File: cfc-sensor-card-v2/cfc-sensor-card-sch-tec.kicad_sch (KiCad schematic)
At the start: 36 parts, among them U12 DRV8212DSGR, U13 AD5593RBCPZ-RL7, U14 MP2410A, U15 INA186A1IDCKR, U16 SN74LVC1G86DBVR, U17 SN74LVC1G08DCKR

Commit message: Processor board routing
Completed rework and routing of processor board. No drc errors or warnings. Ready for design review on processor board. Minor changes to schematic for easier routing on pull down resistors connected to the octavo SIP. Reannotated sensor schematic component designators.
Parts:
- renumbered C67 to C31, C66 to C32, C74 to C33, C68 to C34, C73 to C35, C35 to C36, C39 to C38, C69 to C39, C70 to C41, C72 to C42, C71 to C43, D5 to D4, D6 to D5, D4 to D6, R58 to R59, R66 to R60, R59 to R61, R57 to R62, R61 to R63, R62 to R64, R67 to R65, R60 to R66, R63 to R67, R71 to R68, R68 to R71, U13 to U12, U16 to U13, U17 to U14, U14 to U15, U12 to U16, U15 to U17

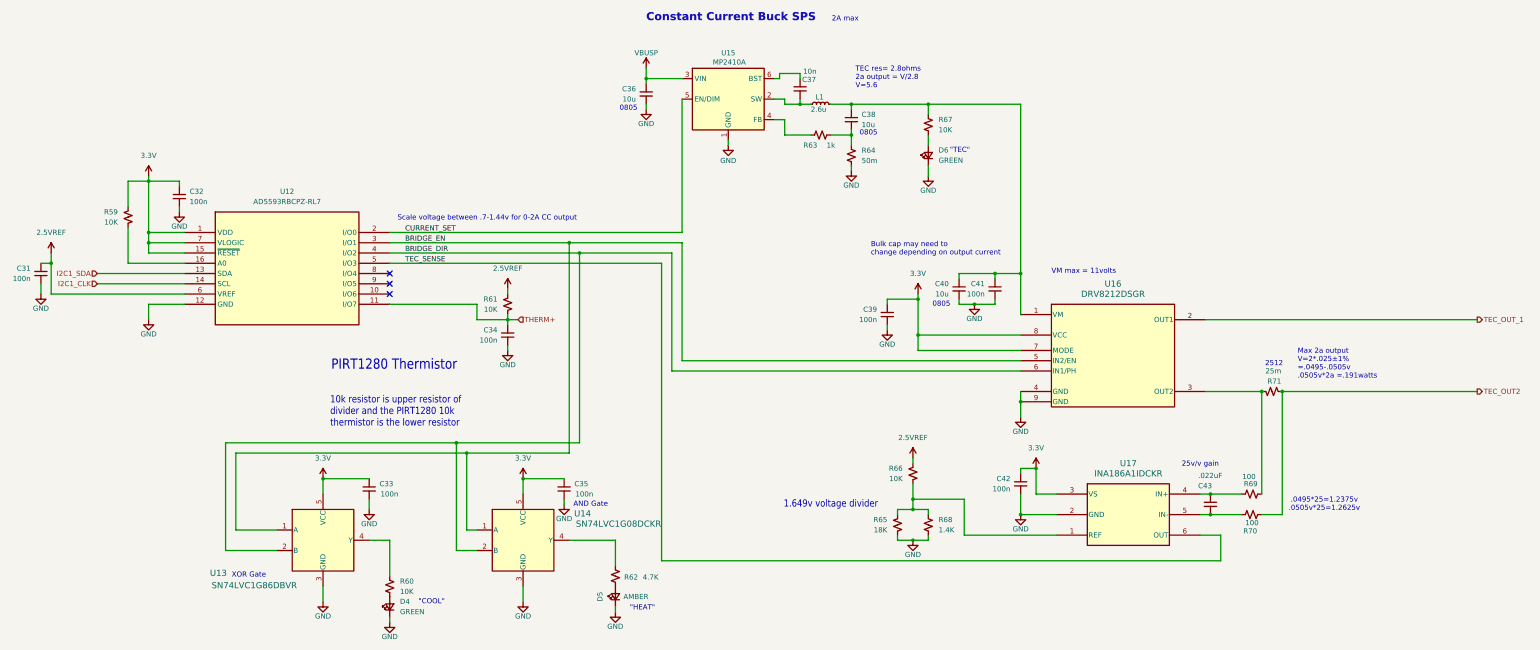
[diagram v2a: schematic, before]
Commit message: Updated OPD on sensor card
updated OPD on sensor card to match protocard. Finished placement on PCB.
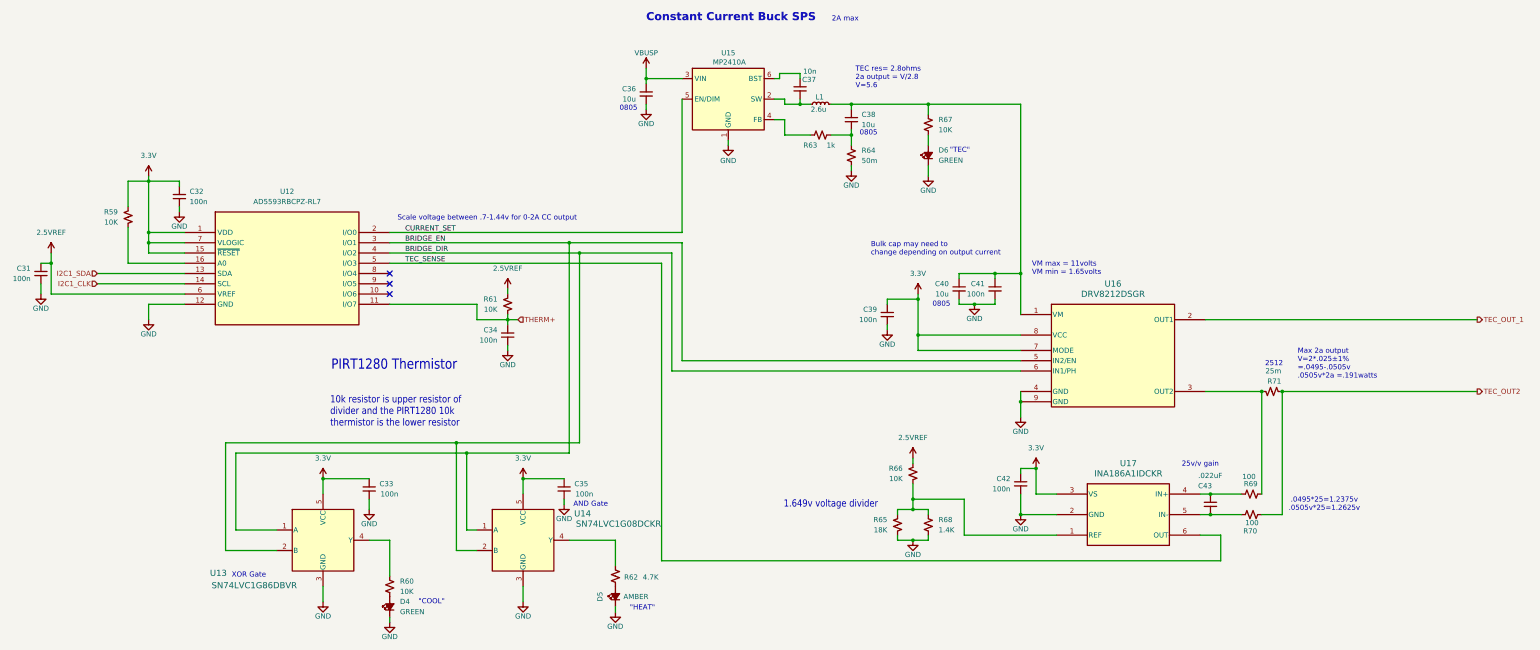
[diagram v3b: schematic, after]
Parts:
- D4, D5, D6: symbol Device:LED_Small -> Device:LED_Small_Filled
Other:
- note added: "VM max = 11volts VM min = 1.65volts"
- note removed: "VM max = 11volts"
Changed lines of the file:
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@@
 		)
 	)
-	(text "VM max = 11volts\n"
+	(text "VM max = 11volts\nVM min = 1.65volts\n"
 		(exclude_from_sim no)
-		(at 273.05 149.352 0)
+		(at 268.224 148.59 0)
 		(effects
 			(font
@@
 	)
 	(symbol
-		(lib_id "Device:LED_Small")
+		(lib_id "Device:LED_Small_Filled")
 		(at 242.57 120.65 90)
 		(unit 1)
@@
 			)
 		)
-		(property "Description" "Light emitting diode, small symbol"
+		(property "Description" "Light emitting diode, small symbol, filled shape"
 			(at 242.57 120.65 0)
 			(hide yes)
@@
 	)
 	(symbol
-		(lib_id "Device:LED_Small")
+		(lib_id "Device:LED_Small_Filled")
 		(at 109.22 232.41 90)
 		(unit 1)
@@
 			)
 		)
-		(property "Description" "Light emitting diode, small symbol"
+		(property "Description" "Light emitting diode, small symbol, filled shape"
 			(at 109.22 232.41 0)
 			(hide yes)
@@
 	)
 	(symbol
-		(lib_name "LED_Small_1")
-		(lib_id "Device:LED_Small")
+		(lib_id "Device:LED_Small_Filled")
 		(at 165.1 229.87 90)
 		(unit 1)
@@
 			)
 		)
-		(property "Description" "Light emitting diode, small symbol"
+		(property "Description" "Light emitting diode, small symbol, filled shape"
 			(at 165.1 229.87 0)
 			(hide yes)

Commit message: Update
Updated BOM, couple of fixes on OPD. Minor routing and layout changes. Removed logic gates from sensor card.
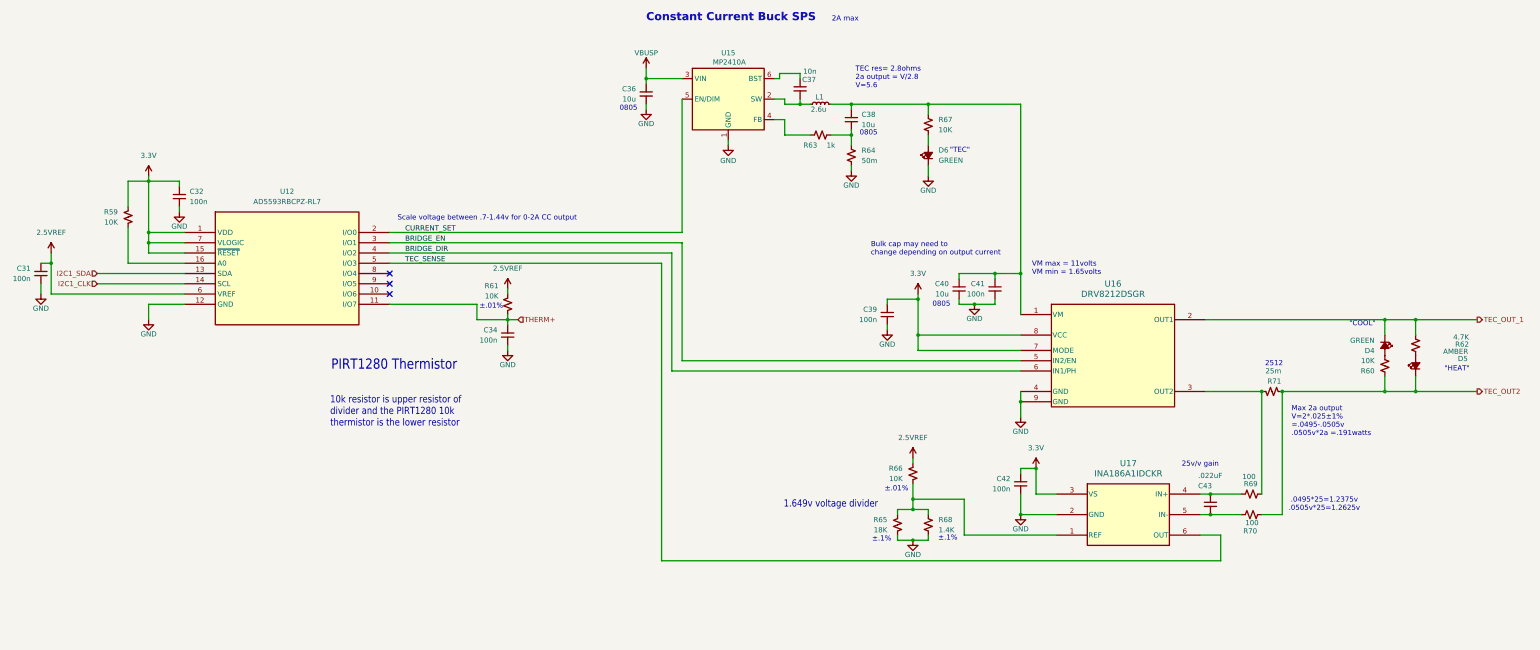
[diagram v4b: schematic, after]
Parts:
- removed C33, C35: 100n, oresat-passives:0603-C-NOSILK, symbol Device:C_Small
- removed U13: SN74LVC1G86DBVR, oresat-ics:DBV5, symbol oresat-ics:SN74LVC1G86DBVR
- removed U14: SN74LVC1G08DCKR, oresat-ics:DCK5-L, symbol oresat-ics:SN74LVC1G08DCKR
- C37: DPN 478-KGM15AR71H103KTCT-ND -> 399-12983-1-ND; MFR KYOCERA AVX -> KEMET; MPN KGM15AR71H103KT -> C0603C103J5RACAUTO
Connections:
- net GND: no longer D4.1 (K), D5.1 (K)
- net TEC_OUT2: now also D5.1 (K), R60.2
- net TEC_OUT_1: now also D4.1 (K), R62.1
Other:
- note added: "±.01%"
- note added: "±.1%"
- note removed: "AND Gate"
- note removed: "XOR Gate"
- moved on the sheet: D4, D5, R60, R62

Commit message: Update
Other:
- note added: "Max 2a output V=2*.025±1% =.0495-.0505v .0505v*2a =.101watts"
- note removed: "Max 2a output V=2*.025±1% =.0495-.0505v .0505v*2a =.191watts"
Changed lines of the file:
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@@
 		)
 	)
-	(text "Max 2a output\nV=2*.025±1%\n=.0495-.0505v\n.0505v*2a =.191watts "
+	(text "Max 2a output\nV=2*.025±1%\n=.0495-.0505v\n.0505v*2a =.101watts "
 		(exclude_from_sim no)
 		(at 332.486 186.436 0)

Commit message: Revert "Update"
This reverts commit deafafed1fe993a788287949c9b0e14f8f1b09d1.
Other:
- note added: "Max 2a output V=2*.025±1% =.0495-.0505v .0505v*2a =.191watts"
- note removed: "Max 2a output V=2*.025±1% =.0495-.0505v .0505v*2a =.101watts"
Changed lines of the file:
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@@
 		)
 	)
-	(text "Max 2a output\nV=2*.025±1%\n=.0495-.0505v\n.0505v*2a =.101watts "
+	(text "Max 2a output\nV=2*.025±1%\n=.0495-.0505v\n.0505v*2a =.191watts "
 		(exclude_from_sim no)
 		(at 332.486 186.436 0)
